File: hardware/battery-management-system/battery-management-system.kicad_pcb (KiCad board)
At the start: 4 copper layers, 100 x 100 mm, 146 parts, among them J1 CELLS, J10 TEMP_CELL3, J11 TEMP_CELL4, J2 Charge, J3 Discharge, J4 VBAT_DISCHARGE, J5 VBAT_CHARGE, J6 AMPHENOL_micro_usb_10118194-0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, J7 ARM-JTAG-SWD, J8 TEMP_CELL1, J9 TEMP_CELL2, Q1 DMN3404L, Q10 DMN3404L, Q11 BS250FTA, Q12 BS250FTA, Q13 BS250FTA, Q14 BS250FTA, Q15 BS250FTA, Q2 TJ40S04M3L, Q3 TJ40S04M3L, Q4 DMN3404L, Q5 DMN3404L, Q6 DMN3404L, Q7 DMN3404L, Q8 DMN3404L, Q9 DMN3404L, U1 ICL7660, U10 LM2904M8-13, U2 L6982CDR, U3 L6982CDR, U4 ICL7660, U5 FT230XS, U6 AT24C512C, U7 NCT75DR2G, U8 STM32L071CZTx, U9 LM2904M8-13

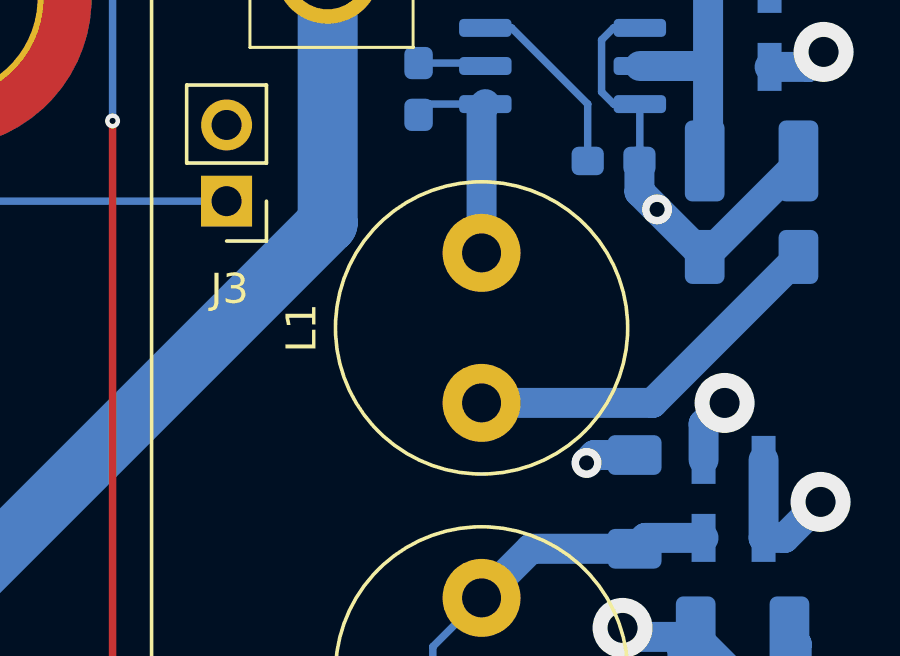
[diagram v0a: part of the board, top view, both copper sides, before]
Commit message: change default board revision for BMS to R01
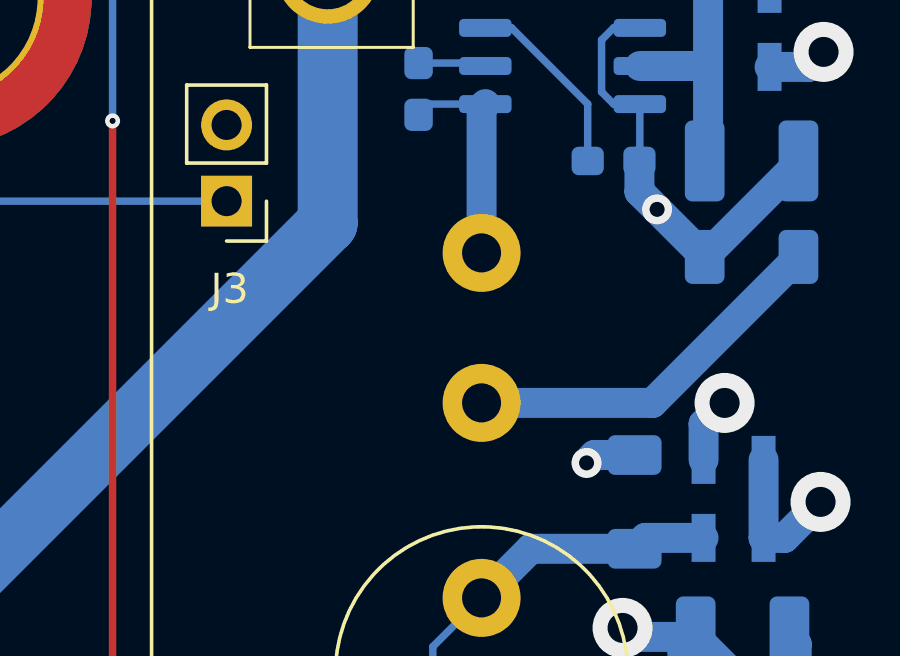
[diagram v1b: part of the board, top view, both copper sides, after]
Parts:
- L1: moved to B.Cu
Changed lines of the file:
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@@
       (net 27 "/MCU/NRST") (pinfunction "B") (pintype "passive"))
-  )
-  (footprint "benediktibk:L_Radial_D9.5mm_P5.00mm_Fastron_07HVP" (layer "F.Cu")
-    (at 106 53.5 90)
-    (descr "Inductor, Radial series, Radial, pin pitch=5.00mm, , diameter=9.5mm, Fastron, 07HVP, http://www.fastrongroup.com/image-show/107/07HVP%2007HVP_T.pdf?type=Complete-DataSheet&productType=series")
-    (tags "Inductor Radial series Radial pin pitch 5.00mm  diameter 9.5mm Fastron 07HVP")
-    (property "RS order number" "800-4388")
-    (property "Sheetfile" "power_supply.kicad_sch")
-    (property "Sheetname" "Power Supply")
-    (property "ki_description" "Inductor")
-    (property "ki_keywords" "inductor choke coil reactor magnetic")
-    (attr through_hole)
-    (fp_text reference "L1" (at 2.5 -6 90) (layer "F.SilkS")
-        (effects (font (size 1 1) (thickness 0.15)))
-    )
-    (fp_text value "22uH" (at 2.96 2.12 90) (layer "F.Fab")
-        (effects (font (size 1 1) (thickness 0.15)))
-    )
-    (fp_text user "${REFERENCE}" (at 2.5 0 90) (layer "F.Fab")
-        (effects (font (size 1 1) (thickness 0.15)))
-    )
-    (fp_circle (center 2.5 0) (end 7.37 0)
-      (stroke (width 0.12) (type solid)) (fill none) (layer "F.SilkS"))
-    (fp_circle (center 2.5 0) (end 7.5 0)
-      (stroke (width 0.05) (type solid)) (fill none) (layer "F.CrtYd"))
-    (fp_circle (center 2.5 0) (end 7.25 0)
-      (stroke (width 0.1) (type solid)) (fill none) (layer "F.Fab"))
-    (pad "1" thru_hole circle (at 0 0 90) (size 2.6 2.6) (drill 1.3) (layers "*.Cu" "*.Mask")
-      (net 5 "/3V3") (pinfunction "1") (pintype "passive"))
-    (pad "2" thru_hole circle (at 5 0 90) (size 2.6 2.6) (drill 1.3) (layers "*.Cu" "*.Mask")
-      (net 12 "Net-(U2-SW)") (pinfunction "2") (pintype "passive"))
-    (model "${KICAD6_3DMODEL_DIR}/Inductor_THT.3dshapes/L_Radial_D9.5mm_P5.00mm_Fastron_07HVP.wrl"
-      (offset (xyz 0 0 0))
-      (scale (xyz 1 1 1))
-      (rotate (xyz 0 0 0))
-    )
   )
   (footprint "benediktibk:rspro_header_4pin_3_5mm" (layer "F.Cu")
@@
       (offset (xyz 0 0 0))
       (scale (xyz 1 1 1))
+      (rotate (xyz 0 0 0))
+    )
+  )
+  (footprint "benediktibk:L_Radial_D9.5mm_P5.00mm_Fastron_07HVP" (layer "B.Cu")
+    (at 106 53.5 90)
+    (descr "Inductor, Radial series, Radial, pin pitch=5.00mm, , diameter=9.5mm, Fastron, 07HVP, http://www.fastrongroup.com/image-show/107/07HVP%2007HVP_T.pdf?type=Complete-DataSheet&productType=series")
+    (tags "Inductor Radial series Radial pin pitch 5.00mm  diameter 9.5mm Fastron 07HVP")
+    (property "RS order number" "800-4388")
+    (property "Sheetfile" "power_supply.kicad_sch")
+    (property "Sheetname" "Power Supply")
+    (property "ki_description" "Inductor")
+    (property "ki_keywords" "inductor choke coil reactor magnetic")
+    (attr through_hole)
+    (fp_text reference "L1" (at 2.5 6 90) (layer "B.SilkS")
+        (effects (font (size 1 1) (thickness 0.15)) (justify mirror))
+    )
+    (fp_text value "22uH" (at 2.96 -2.12 90) (layer "B.Fab")
+        (effects (font (size 1 1) (thickness 0.15)) (justify mirror))
+    )
+    (fp_text user "${REFERENCE}" (at 2.5 0 90) (layer "B.Fab")
+        (effects (font (size 1 1) (thickness 0.15)) (justify mirror))
+    )
+    (fp_circle (center 2.5 0) (end 7.37 0)
+      (stroke (width 0.12) (type solid)) (fill none) (layer "B.SilkS"))
+    (fp_circle (center 2.5 0) (end 7.5 0)
+      (stroke (width 0.05) (type solid)) (fill none) (layer "B.CrtYd"))
+    (fp_circle (center 2.5 0) (end 7.25 0)
+      (stroke (width 0.1) (type solid)) (fill none) (layer "B.Fab"))
+    (pad "1" thru_hole circle (at 0 0 90) (size 2.6 2.6) (drill 1.3) (layers "*.Cu" "*.Mask")
+      (net 5 "/3V3") (pinfunction "1") (pintype "passive"))
+    (pad "2" thru_hole circle (at 5 0 90) (size 2.6 2.6) (drill 1.3) (layers "*.Cu" "*.Mask")
+      (net 12 "Net-(U2-SW)") (pinfunction "2") (pintype "passive"))
+    (model "${KICAD6_3DMODEL_DIR}/Inductor_THT.3dshapes/L_Radial_D9.5mm_P5.00mm_Fastron_07HVP.wrl"
+      (offset (xyz 0 0 0))
+      (scale (xyz 1 1 1))

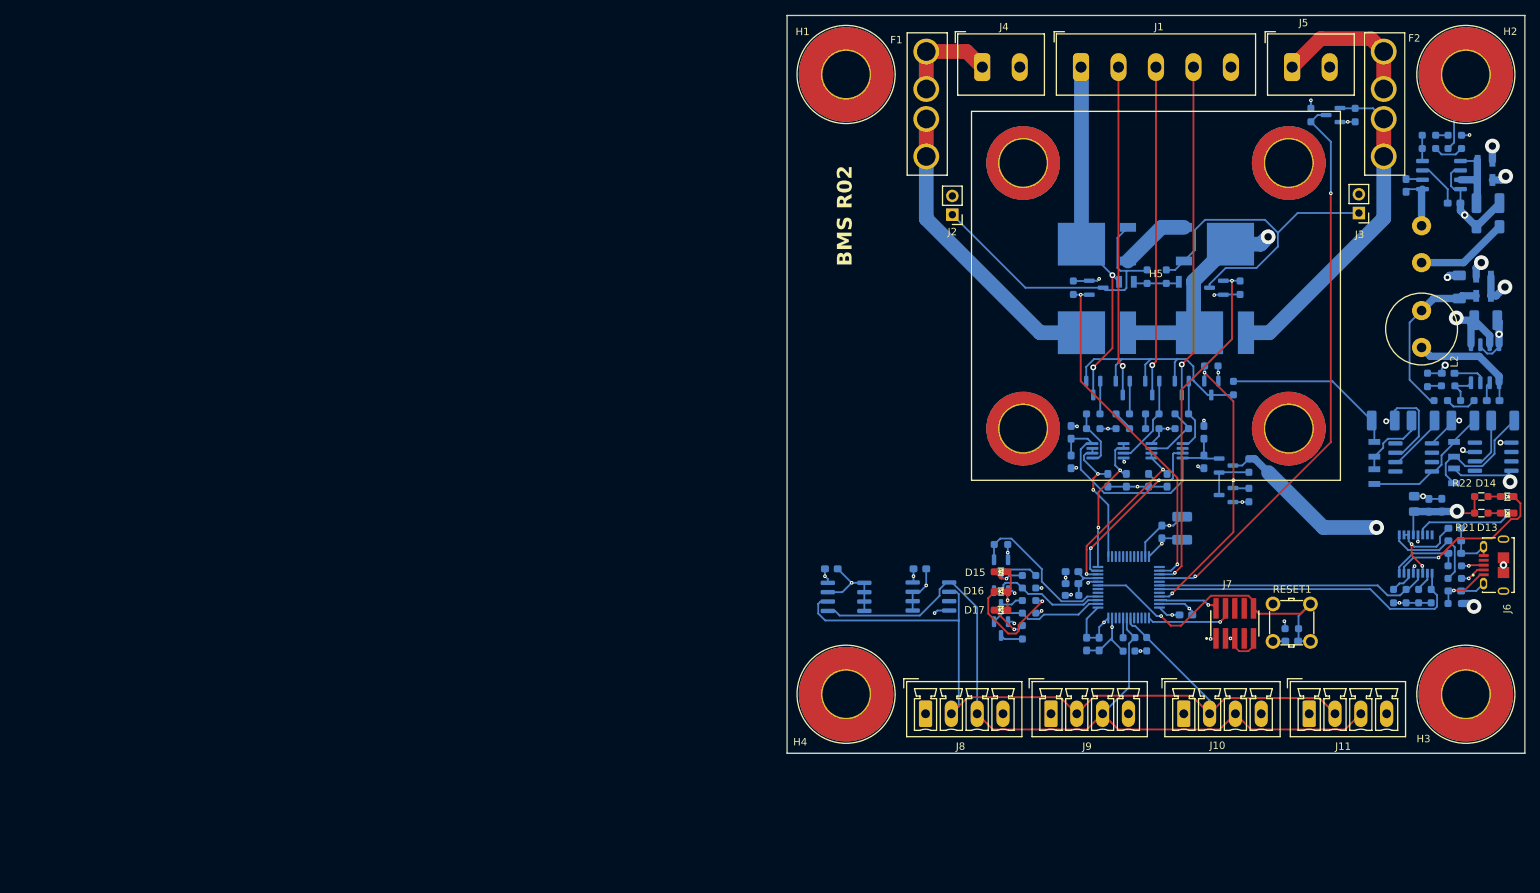
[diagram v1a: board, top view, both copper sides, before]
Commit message: fix design errors of battery management system R02
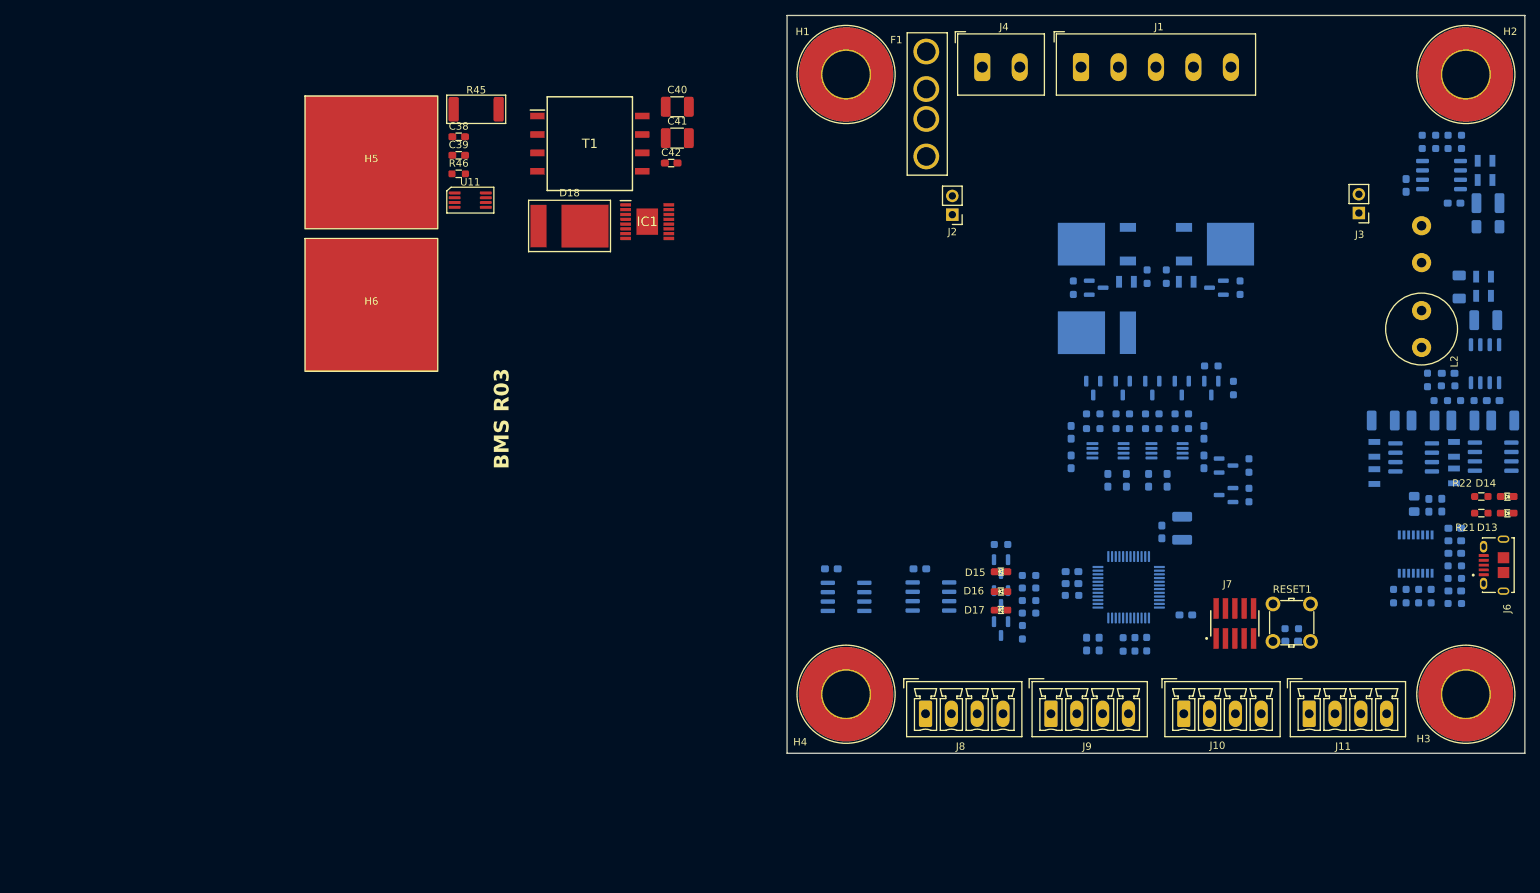
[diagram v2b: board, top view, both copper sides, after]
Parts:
- removed D4: SBR2065D1, benediktibk:SBR2065D1
- removed F2: 20A, benediktibk:KEYSTONE_blade_fus_holder
- removed J5: VBAT_CHARGE, benediktibk:rspro_header_2pin_5_08mm
- removed Q5: DMN3404L, benediktibk:SOT-23
- removed R5, R6: 10kOhm, benediktibk:R_0603_1608Metric_Pad0.98x0.95mm_HandSolder
- added C38: 1uF, benediktibk:C_0603_1608Metric_Pad1.08x0.95mm_HandSolder, F.Cu at (-24.5, 36.4)
- added C39: 100nF, benediktibk:C_0603_1608Metric_Pad1.08x0.95mm_HandSolder, F.Cu at (-24.5, 39.0)
- added C40: 10uF, benediktibk:C_1210_3225Metric_Pad1.33x2.70mm_HandSolder, F.Cu at (5.12, 32.4)
- added C41: 10uF, benediktibk:C_1210_3225Metric_Pad1.33x2.70mm_HandSolder, F.Cu at (5.12, 36.6)
- added C42: 1uF, benediktibk:C_0603_1608Metric_Pad1.08x0.95mm_HandSolder, F.Cu at (4.29, 40.0)
- added D18: SBR2065D1, benediktibk:SBR2065D1, F.Cu at (-9.48, 48.5)
- added H6: heatsink_18x18, benediktibk:heatsink_18x18, F.Cu at (-36.3, 59.2)
- added IC1: LT8584EFE#PBF, benediktibk:SOP65P640X110-17N, F.Cu at (1.04, 48.0)
- added R45: 2mOhm/5W, benediktibk:R_2512_6332Metric_Pad1.40x3.35mm_HandSolder, F.Cu at (-22.1, 32.7)
- added R46: 200kOhm, benediktibk:R_0603_1608Metric_Pad0.98x0.95mm_HandSolder, F.Cu at (-24.5, 41.5)
- added T1: NA6252-ALD, benediktibk:SOP250P1524X1143-8N, F.Cu at (-6.73, 37.4)
- added U11: STC3100, benediktibk:MSOP-8_3x3mm_P0.65mm, F.Cu at (-22.9, 45.0)
- H5: value heatsink_50x50 -> heatsink_18x18; footprint benediktibk:heatsink_50x50 -> benediktibk:heatsink_18x18
- moved H5 107.9 mm to (-36.3, 39.9)
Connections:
- D3 pad 1: /PACK_EXT -> GND
- D3 pad 2: Net-(D3-K) -> /PACK_EXT
- F1 pad 2: Net-(D3-K) -> /PACK_EXT
- J1 pad 5: GND -> /Battery Pack/CELL1_MINUS
- R39 pad 2: Net-(R39-Pad2) -> Net-(U9A-+)
- R40 pad 1: Net-(R39-Pad2) -> Net-(U9A-+)
- R41 pad 2: Net-(R41-Pad2) -> Net-(U10B-+)
- R42 pad 1: Net-(R41-Pad2) -> Net-(U10B-+)
- U10 pad 5: Net-(Q15-D) -> Net-(U10B-+)
- U8 pad 28: /Battery Pack/CHARGE_AVAILABLE -> /MCU/CHARGE_AVAILABLE
- U9 pad 3: Net-(Q14-D) -> Net-(U9A-+)
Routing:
- net GND: track 173.1 -> 0.00 mm, vias 39 -> 0
- net /MCU/SCL: track 115.5 -> 0.00 mm
- net /MCU/SDA: track 111.2 -> 0.00 mm
- net /Battery Pack/CHARGE_AVAILABLE: track 77.8 -> 0.00 mm, vias 2 -> 0
- net /3V3: track 52.5 -> 0.00 mm, vias 13 -> 0
- net /Battery Pack/PACK: track 48.6 -> 0.00 mm, vias 2 -> 0
- net /DISCHARGE: track 47.3 -> 0.00 mm, vias 2 -> 0
- net /CHARGE: track 46.9 -> 0.00 mm, vias 2 -> 0
- net Net-(J3-Pin_1): track 46.1 -> 0.00 mm
- net Net-(D4-A): track 45.1 -> 0.00 mm
- net /Battery Pack/CELL2_MINUS: track 45.1 -> 0.00 mm, vias 1 -> 0
- net /Battery Pack/CELL4_MINUS: track 44.7 -> 0.00 mm, vias 1 -> 0
- net /Battery Pack/CELL3_MINUS: track 44.6 -> 0.00 mm, vias 1 -> 0
- net /MCU/UART_USB_RX: track 43.8 -> 0.00 mm
- net /MCU/NRST: track 42.3 -> 0.00 mm, vias 1 -> 0
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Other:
- board text added: "BMS R03"
- board text removed: "BMS R02"
